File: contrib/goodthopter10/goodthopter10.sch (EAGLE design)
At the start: 11 parts, among them IC1 F22X4---DA38, IC2 FT232RL-BASICSSOP, X1 USBPCB

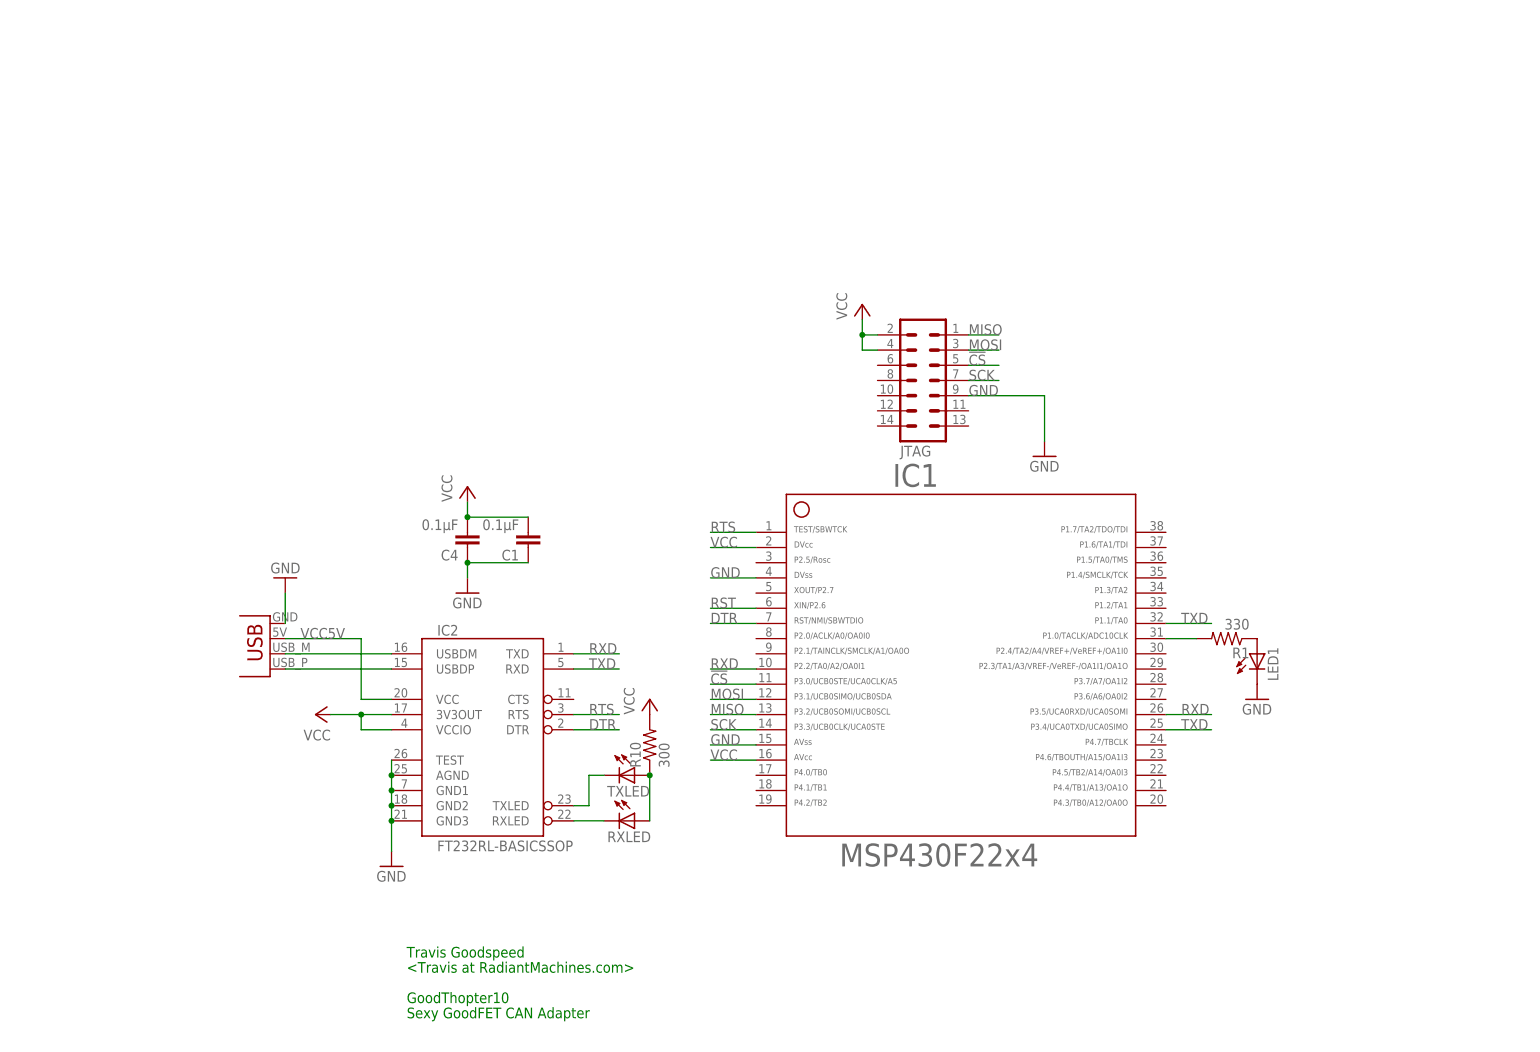
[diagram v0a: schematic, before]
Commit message: goodthopter10 schematic progress, mcp done and routed
git-svn-id: https://svn.code.sf.net/p/goodfet/code@1194 12e2690d-a6be-4b82-a7b7-67c4a43b65c8
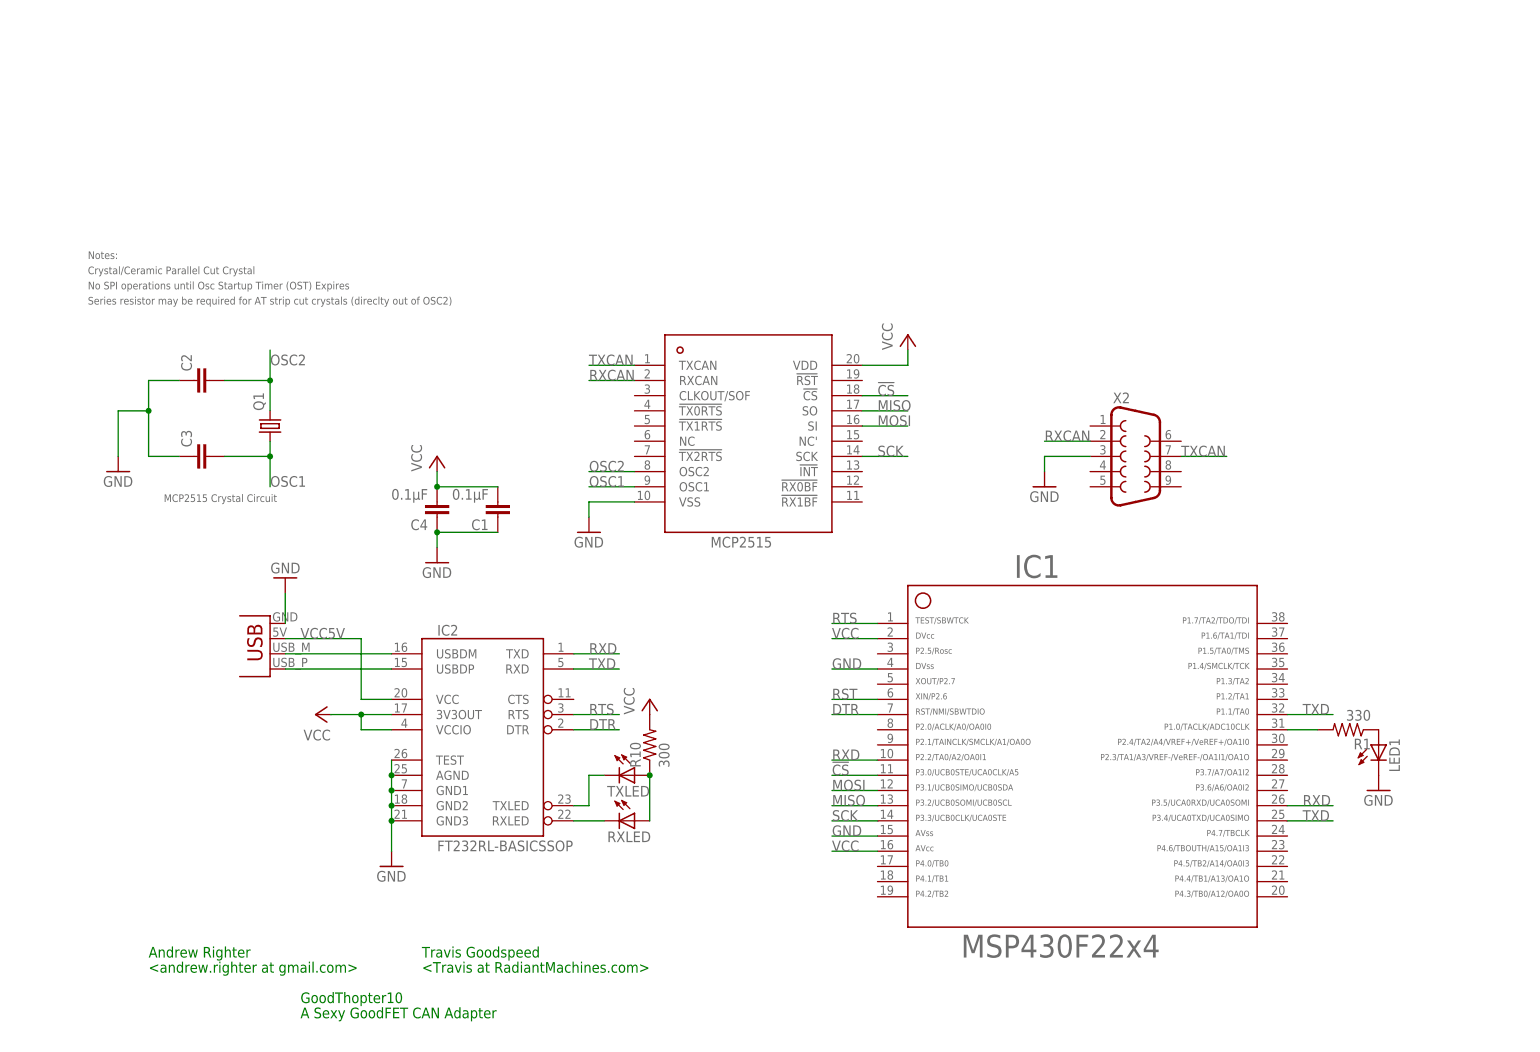
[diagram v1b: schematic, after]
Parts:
- removed JTAG: (no value), con-lstb:MA07-2
- added C2, C3: (no value), rcl:C-EUC0603
- added Q1: (no value), crystal:CRYSTALMM20SS
- added U$1: MCP2515, MCP2515:MCP2515
- added X2: (no value), SparkFun-Connectors:DB9MALE
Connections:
- new net OSC1: C3.2, Q1.1, U$1.OSC1
- new net OSC2: C2.2, Q1.2, U$1.OSC2
- new net RXCAN: U$1.RXCAN, X2.2
- new net TXCAN: U$1.TXCAN, X2.7
- net !CS: now also U$1.!CS; no longer JTAG.5
- net GND: now also C2.1, C3.1, U$1.VSS, X2.3; no longer JTAG.9
- net MISO: now also U$1.SO; no longer JTAG.1
- net MOSI: now also U$1.SI; no longer JTAG.3
- net SCK: now also U$1.SCK; no longer JTAG.7
- net VCC: now also U$1.VDD; no longer JTAG.2, JTAG.4
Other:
- note added: "<andrew.righter at gmail.com>"
- note added: "A Sexy GoodFET CAN Adapter"
- note added: "Andrew Righter"
- note added: "Crystal/Ceramic Parallel Cut Crystal"
- note added: "MCP2515 Crystal Circuit"
- note added: "No SPI operations until Osc Startup Timer (OST) Expires"
- note added: "Notes:"
- note added: "Series resistor may be required for AT strip cut crystals (direclty out of OSC2)"
- note removed: "Sexy GoodFET CAN Adapter"
- moved on the sheet: C1, C4, IC1, LED1, R1

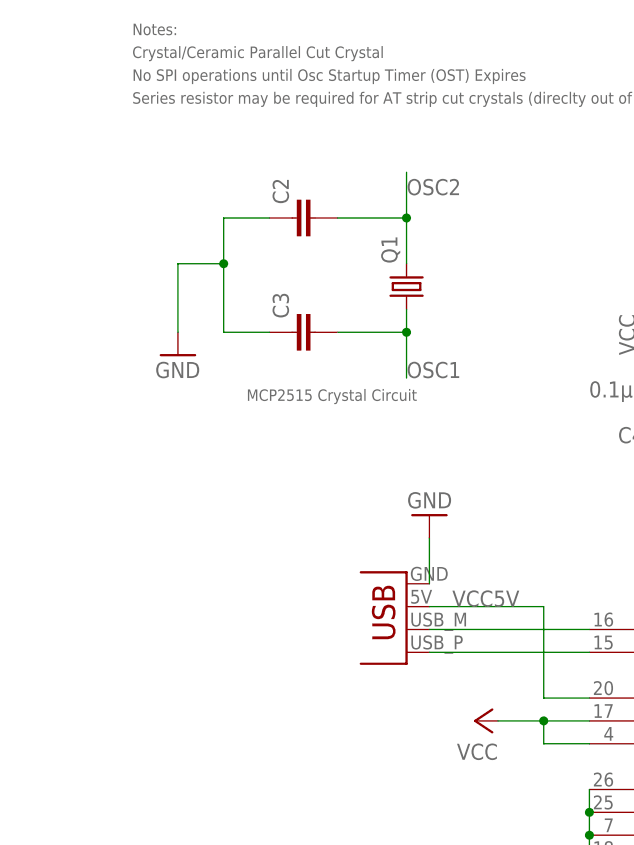
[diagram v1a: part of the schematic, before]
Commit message: Updated values for crystal circuit (MCP2515).
git-svn-id: https://svn.code.sf.net/p/goodfet/code@1195 12e2690d-a6be-4b82-a7b7-67c4a43b65c8
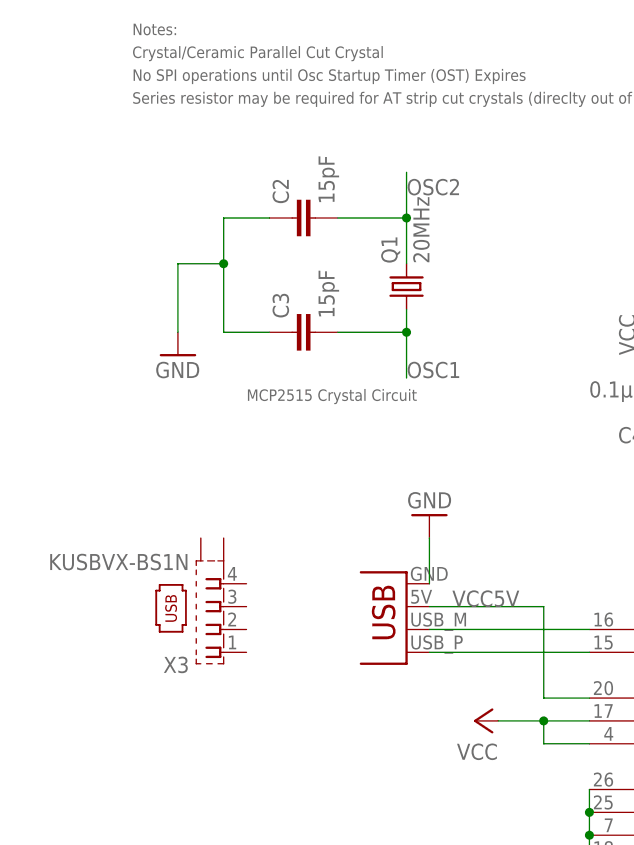
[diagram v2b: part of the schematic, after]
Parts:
- added X3: KUSBVX-BS1N, con-kycon:KUSBVX-BS1N
- C2, C3: value (none) -> 15pF
- Q1: value (none) -> 20MHz
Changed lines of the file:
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@@
 <grid distance="0.1" unitdist="inch" unit="inch" style="lines" multiple="1" display="no" altdistance="0.01" altunitdist="inch" altunit="inch"/>
 <layers>
-<layer number="1" name="Top" color="4" fill="1" visible="yes" active="no"/>
-<layer number="16" name="Bottom" color="1" fill="1" visible="yes" active="no"/>
-<layer number="17" name="Pads" color="2" fill="1" visible="yes" active="no"/>
-<layer number="18" name="Vias" color="2" fill="1" visible="yes" active="no"/>
-<layer number="19" name="Unrouted" color="6" fill="1" visible="yes" active="no"/>
-<layer number="20" name="Dimension" color="15" fill="1" visible="yes" active="no"/>
-<layer number="21" name="tPlace" color="7" fill="1" visible="yes" active="no"/>
-<layer number="22" name="bPlace" color="7" fill="1" visible="yes" active="no"/>
-<layer number="23" name="tOrigins" color="15" fill="1" visible="yes" active="no"/>
-<layer number="24" name="bOrigins" color="15" fill="1" visible="yes" active="no"/>
-<layer number="25" name="tNames" color="7" fill="1" visible="yes" active="no"/>
-<layer number="26" name="bNames" color="7" fill="1" visible="yes" active="no"/>
-<layer number="27" name="tValues" color="7" fill="1" visible="yes" active="no"/>
-<layer number="28" name="bValues" color="7" fill="1" visible="yes" active="no"/>
+<layer number="1" name="Top" color="4" fill="1" visible="no" active="no"/>
+<layer number="16" name="Bottom" color="1" fill="1" visible="no" active="no"/>
+<layer number="17" name="Pads" color="2" fill="1" visible="no" active="no"/>
+<layer number="18" name="Vias" color="2" fill="1" visible="no" active="no"/>
+<layer number="19" name="Unrouted" color="6" fill="1" visible="no" active="no"/>
+<layer number="20" name="Dimension" color="15" fill="1" visible="no" active="no"/>
+<layer number="21" name="tPlace" color="7" fill="1" visible="no" active="no"/>
+<layer number="22" name="bPlace" color="7" fill="1" visible="no" active="no"/>
+<layer number="23" name="tOrigins" color="15" fill="1" visible="no" active="no"/>
+<layer number="24" name="bOrigins" color="15" fill="1" visible="no" active="no"/>
+<layer number="25" name="tNames" color="7" fill="1" visible="no" active="no"/>
+<layer number="26" name="bNames" color="7" fill="1" visible="no" active="no"/>
+<layer number="27" name="tValues" color="7" fill="1" visible="no" active="no"/>
+<layer number="28" name="bValues" color="7" fill="1" visible="no" active="no"/>
 <layer number="29" name="tStop" color="7" fill="3" visible="no" active="no"/>
 <layer number="30" name="bStop" color="7" fill="6" visible="no" active="no"/>
@@
 <layer number="35" name="tGlue" color="7" fill="4" visible="no" active="no"/>
 <layer number="36" name="bGlue" color="7" fill="5" visible="no" active="no"/>
-<layer number="37" name="tTest" color="7" fill="1" visible="yes" active="no"/>
-<layer number="38" name="bTest" color="7" fill="1" visible="yes" active="no"/>
+<layer number="37" name="tTest" color="7" fill="1" visible="no" active="no"/>
+<layer number="38" name="bTest" color="7" fill="1" visible="no" active="no"/>
 <layer number="39" name="tKeepout" color="4" fill="11" visible="no" active="no"/>
 <layer number="40" name="bKeepout" color="1" fill="11" visible="no" active="no"/>
@@
 <layer number="44" name="Drills" color="7" fill="1" visible="no" active="no"/>
 <layer number="45" name="Holes" color="7" fill="1" visible="no" active="no"/>
-<layer number="46" name="Milling" color="3" fill="1" visible="yes" active="no"/>
-<layer number="47" name="Measures" color="7" fill="1" visible="yes" active="no"/>
-<layer number="48" name="Document" color="7" fill="1" visible="yes" active="no"/>
-<layer number="49" name="Reference" color="7" fill="1" visible="yes" active="no"/>
-<layer number="50" name="dxf" color="7" fill="1" visible="yes" active="no"/>
-<layer number="51" name="tDocu" color="7" fill="1" visible="yes" active="no"/>
-<layer number="52" name="bDocu" color="7" fill="1" visible="yes" active="no"/>
-<layer number="53" name="tGND_GNDA" color="7" fill="9" visible="yes" active="no"/>
-<layer number="54" name="bGND_GNDA" color="1" fill="9" visible="yes" active="no"/>
-<layer number="56" name="wert" color="7" fill="1" visible="yes" active="no"/>
+<layer number="46" name="Milling" color="3" fill="1" visible="no" active="no"/>
+<layer number="47" name="Measures" color="7" fill="1" visible="no" active="no"/>
+<layer number="48" name="Document" color="7" fill="1" visible="no" active="no"/>
+<layer number="49" name="Reference" color="7" fill="1" visible="no" active="no"/>
+<layer number="50" name="dxf" color="7" fill="1" visible="no" active="no"/>
+<layer number="51" name="tDocu" color="7" fill="1" visible="no" active="no"/>
+<layer number="52" name="bDocu" color="7" fill="1" visible="no" active="no"/>
+<layer number="53" name="tGND_GNDA" color="7" fill="9" visible="no" active="no"/>
+<layer number="54" name="bGND_GNDA" color="1" fill="9" visible="no" active="no"/>
+<layer number="56" name="wert" color="7" fill="1" visible="no" active="no"/>
 <layer number="91" name="Nets" color="2" fill="1" visible="yes" active="yes"/>
 <layer number="92" name="Busses" color="1" fill="1" visible="yes" active="yes"/>
@@
 <part name="C1" library="rcl" deviceset="C-EU" device="C0603" value="0.1µF"/>
 <part name="U$1" library="MCP2515" deviceset="MCP2515" device=""/>
-<part name="C2" library="rcl" deviceset="C-EU" device="C0603"/>
-<part name="C3" library="rcl" deviceset="C-EU" device="C0603"/>
+<part name="C2" library="rcl" deviceset="C-EU" device="C0603" value="15pF"/>
+<part name="C3" library="rcl" deviceset="C-EU" device="C0603" value="15pF"/>
 <part name="GND1" library="supply1" deviceset="GND" device=""/>
 <part name="X2" library="SparkFun-Connectors" deviceset="DB9" device="MALE"/>
-<part name="Q1" library="crystal" deviceset="CRYSTAL" device="MM20SS"/>
+<part name="Q1" library="crystal" deviceset="CRYSTAL" device="MM20SS" value="20MHz"/>
 <part name="GND2" library="supply1" deviceset="GND" device=""/>
 <part name="GND6" library="supply1" deviceset="GND" device=""/>
 <part name="P+1" library="supply1" deviceset="VCC" device=""/>
+<part name="X3" library="con-kycon" deviceset="KUSBVX-BS1N" device=""/>
 </parts>
 <sheets>
@@
 <instance part="GND6" gate="1" x="30.48" y="86.36"/>
 <instance part="P+1" gate="VCC" x="83.82" y="119.38"/>
+<instance part="X3" gate="G$1" x="-45.72" y="68.58" rot="R180"/>
 </instances>
 <busses>

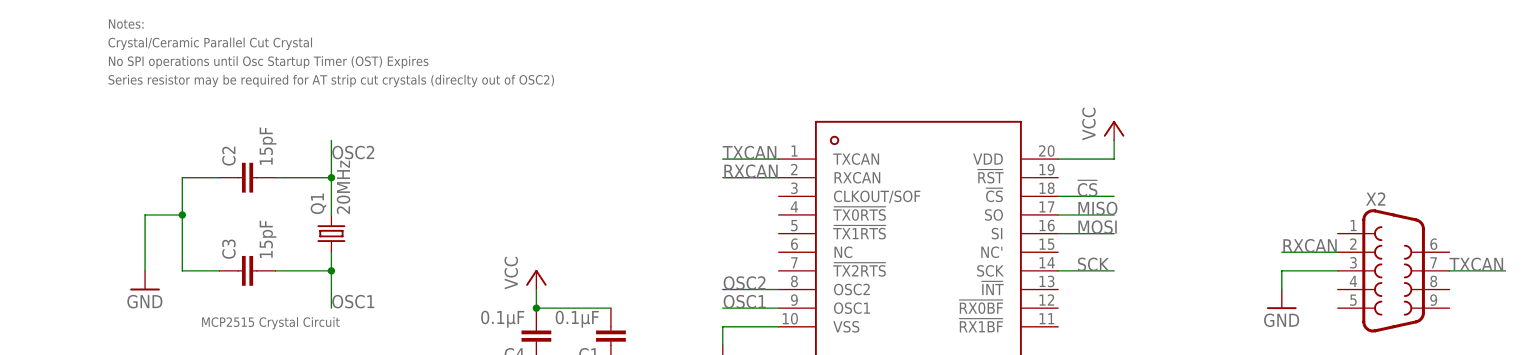
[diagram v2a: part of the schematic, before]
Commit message: Updated goodthopter schematic, fixing CAN physical connector.
git-svn-id: https://svn.code.sf.net/p/goodfet/code@1196 12e2690d-a6be-4b82-a7b7-67c4a43b65c8
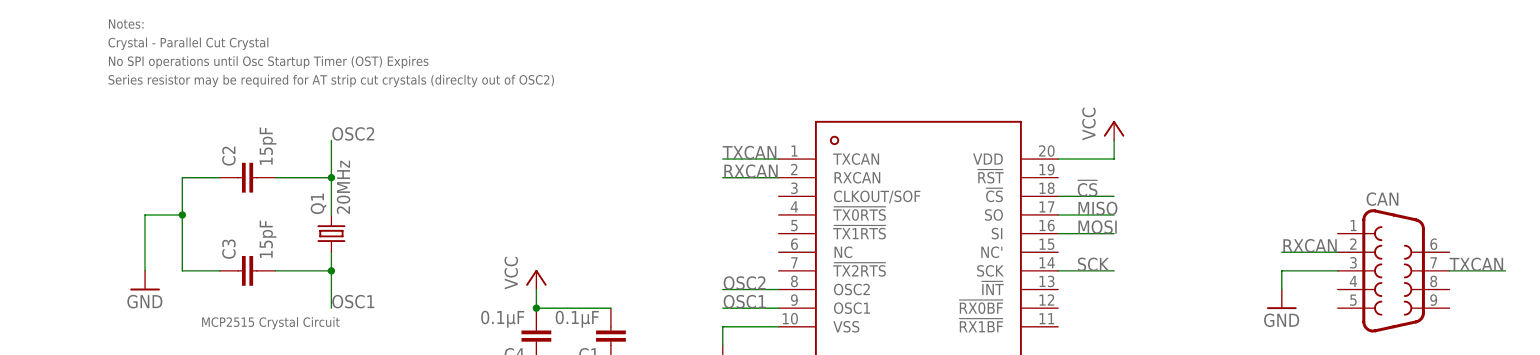
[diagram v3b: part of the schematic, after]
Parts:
- renumbered X2 to CAN
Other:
- note added: "Crystal - Parallel Cut Crystal"
- note removed: "Crystal/Ceramic Parallel Cut Crystal"
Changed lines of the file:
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@@
 <part name="C3" library="rcl" deviceset="C-EU" device="C0603" value="15pF"/>
 <part name="GND1" library="supply1" deviceset="GND" device=""/>
-<part name="X2" library="SparkFun-Connectors" deviceset="DB9" device="MALE"/>
+<part name="CAN" library="SparkFun-Connectors" deviceset="DB9" device="MALE"/>
 <part name="Q1" library="crystal" deviceset="CRYSTAL" device="MM20SS" value="20MHz"/>
 <part name="GND2" library="supply1" deviceset="GND" device=""/>
@@
 <text x="-43.18" y="15.24" size="1.778" layer="91">Andrew Righter</text>
 <text x="-43.18" y="12.7" size="1.778" layer="91">&lt;andrew.righter at gmail.com&gt;</text>
-<text x="-53.34" y="129.54" size="1.27" layer="95">Crystal/Ceramic Parallel Cut Crystal</text>
+<text x="-53.34" y="129.54" size="1.27" layer="95">Crystal - Parallel Cut Crystal</text>
 <text x="-53.34" y="132.08" size="1.27" layer="95">Notes:</text>
 <text x="-53.34" y="127" size="1.27" layer="95">No SPI operations until Osc Startup Timer (OST) Expires</text>
@@
 <instance part="C3" gate="G$1" x="-35.56" y="99.06" rot="R90"/>
 <instance part="GND1" gate="1" x="-48.26" y="96.52"/>
-<instance part="X2" gate="G$1" x="121.92" y="99.06"/>
+<instance part="CAN" gate="G$1" x="121.92" y="99.06"/>
 <instance part="Q1" gate="G$1" x="-22.86" y="104.14" rot="R90"/>
 <instance part="GND2" gate="1" x="106.68" y="93.98"/>
@@
 </segment>
 <segment>
-<pinref part="X2" gate="G$1" pin="3"/>
+<pinref part="CAN" gate="G$1" pin="3"/>
 <wire x1="114.3" y1="99.06" x2="106.68" y2="99.06" width="0.1524" layer="91"/>
 <pinref part="GND2" gate="1" pin="GND"/>
@@
 <wire x1="-30.48" y1="111.76" x2="-22.86" y2="111.76" width="0.1524" layer="91"/>
 <wire x1="-22.86" y1="111.76" x2="-22.86" y2="116.84" width="0.1524" layer="91"/>
-<label x="-22.86" y="114.3" size="1.778" layer="95"/>
+<label x="-22.86" y="116.84" size="1.778" layer="95"/>
 <pinref part="Q1" gate="G$1" pin="2"/>
 <wire x1="-22.86" y1="106.68" x2="-22.86" y2="111.76" width="0.1524" layer="91"/>
@@
 </segment>
 <segment>
-<pinref part="X2" gate="G$1" pin="7"/>
+<pinref part="CAN" gate="G$1" pin="7"/>
 <wire x1="129.54" y1="99.06" x2="137.16" y2="99.06" width="0.1524" layer="91"/>
 <label x="129.54" y="99.06" size="1.778" layer="95"/>
@@
 </segment>
 <segment>
-<pinref part="X2" gate="G$1" pin="2"/>
+<pinref part="CAN" gate="G$1" pin="2"/>
 <wire x1="114.3" y1="101.6" x2="106.68" y2="101.6" width="0.1524" layer="91"/>
 <label x="106.68" y="101.6" size="1.778" layer="95"/>
